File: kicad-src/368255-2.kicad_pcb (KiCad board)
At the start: 2 copper layers, 158 x 114 mm, 27 parts, among them J11 5569-08A2, J2 5569-18A2, J21 Conn_01x01_Pin, J22 Conn_01x01_Pin, J23 Conn_01x01_Pin, J24 Conn_01x01_Pin, J25 Conn_01x01_Pin, J26 Conn_01x01_Pin, J27 Conn_01x01_Pin, J28 Conn_01x01_Pin, J3 5569-06A2, J4 5569-16A2, J5 5569-20A2, P1 368255-2, U1 ULN2003A

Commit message: tracing refinement
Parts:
- added R10: 10k, Resistor_SMD:R_0201_0603Metric, F.Cu at (178.8, 92.0)
- added R8: 10k, Resistor_SMD:R_0201_0603Metric, F.Cu at (178.8, 93.0)
- added R9: 10k, Resistor_SMD:R_0201_0603Metric, F.Cu at (178.8, 90.6)
- J5: value 5569-20A2 -> 5569-20A2-new
- moved J25 1.45 mm to (169.3, 104.8)
- moved R1 0.80 mm to (172.9, 102.5), turned to 90 degrees
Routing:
- net /OUT_IGN1: track 144.2 -> 131.5 mm
- net GND: track 248.4 -> 254.8 mm
- net /BUTTON3: track 52.8 -> 58.7 mm
- net /OUT_INJ4: track 73.3 -> 67.7 mm
- net /IN_PPS2: track 175.6 -> 170.5 mm
- net /IN_BUTTON2: track 55.6 -> 59.0 mm
- net /OUT_DC2+: track 61.5 -> 58.7 mm
- net /CONTITIONER_ON: track 83.9 -> 86.3 mm
- net /5_WBO_Rtrim: track 146.4 -> 144.1 mm
- net /BUTTON1: track 50.6 -> 52.9 mm
- net +5VP: track 310.9 -> 309.4 mm
- net /CLUTCH_SENSOR: track 42.3 -> 43.7 mm
- net /OUT_IGN3: track 247.1 -> 245.8 mm
- net Net-(J25-Pin_1): track 8.99 -> 8.09 mm
- net /OUT_IGN2: track 151.2 -> 152.1 mm
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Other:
- board text added: "+5V_USB"
- board text added: "D+"
- board text added: "D-"
- board text added: "GND"

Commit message: tracing
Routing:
- net /OUT_LS3: track 73.7 -> 68.9 mm, vias 1 -> 0
- net GNDA: track 251.1 -> 246.8 mm
- net /5_WBO_Rtrim: track 144.1 -> 145.8 mm
- net /IN_BUTTON2: track 59.0 -> 57.5 mm
- net GND: track 254.8 -> 253.7 mm
- net /OUT_IGN5: track 50.0 -> 49.4 mm

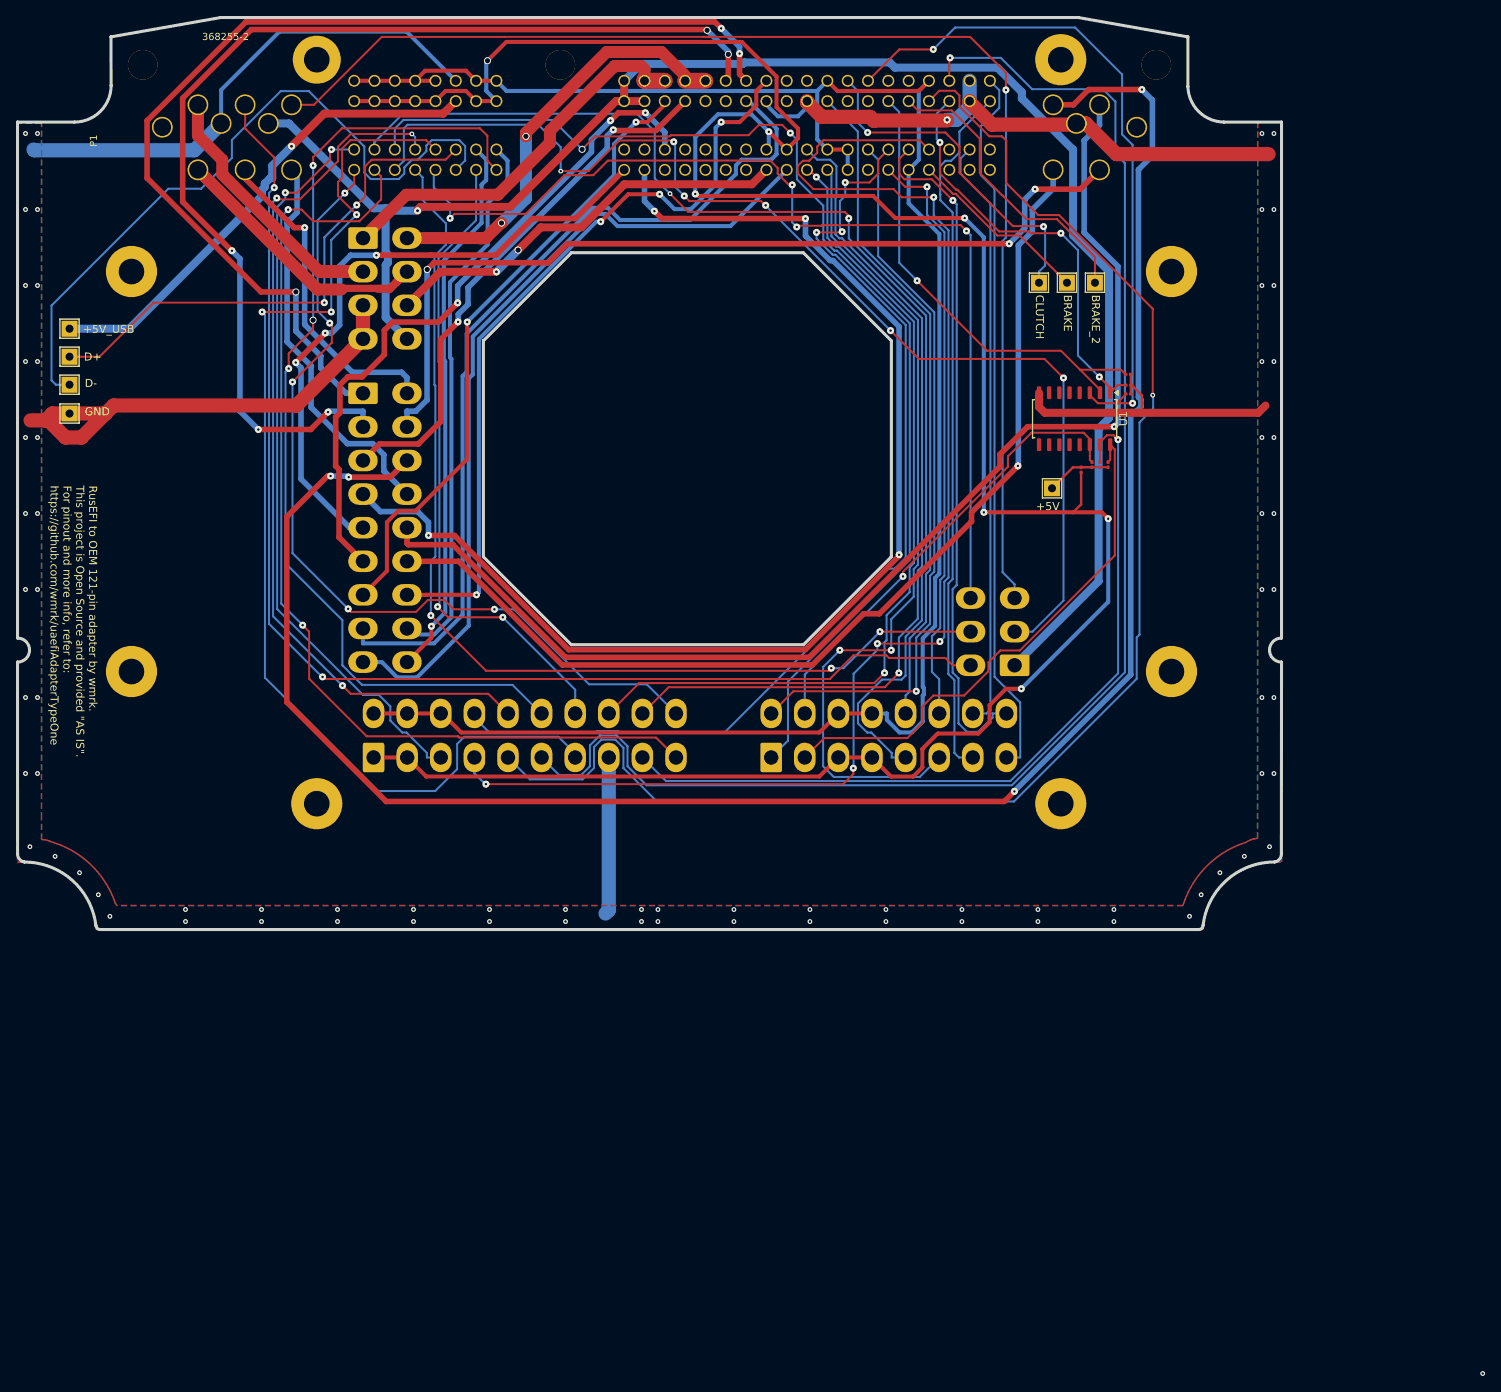
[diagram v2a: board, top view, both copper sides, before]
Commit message: net classes global fix
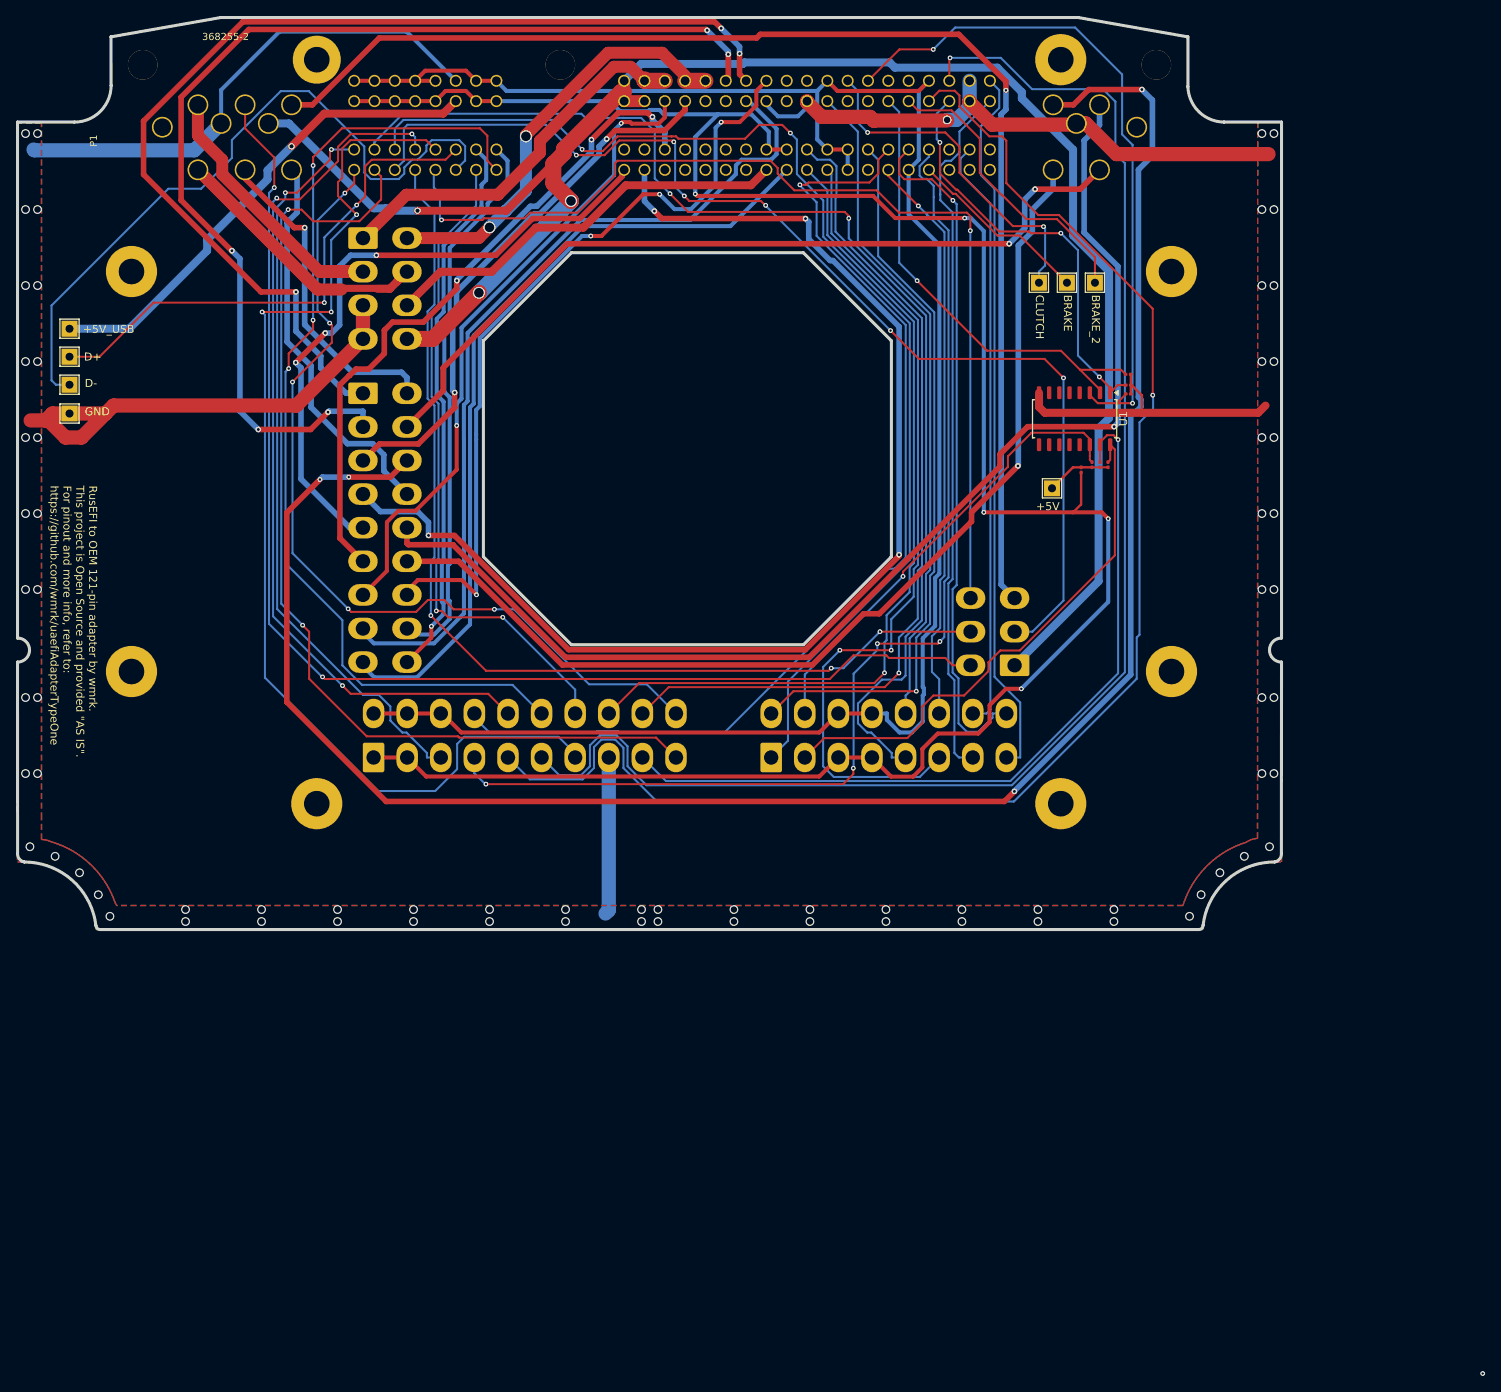
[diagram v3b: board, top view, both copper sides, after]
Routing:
- net /3_WBO_Heater: track 161.2 -> 202.4 mm
- net /IN_PPS2: track 170.5 -> 140.1 mm, vias 5 -> 4
- net +5VP: track 308.9 -> 281.9 mm, vias 7 -> 5
- net +12V: track 210.7 -> 227.0 mm, vias 1 -> 3
- net /OUT_IGN4: track 112.7 -> 103.6 mm, vias 3 -> 2
- net /5_WBO_Rtrim: track 145.8 -> 142.4 mm
- net /IN_TPS2: track 127.7 -> 130.3 mm, vias 3 -> 1
- net /OUT_LS1: track 79.4 -> 81.5 mm
- net /OUT_LS_HOT2: track 109.5 -> 107.4 mm
- net /OUT_LS4: track 96.9 -> 98.7 mm
- net /IN_KNOCK_RAW: track 73.5 -> 71.9 mm
- net /VR_MAX9924-: track 81.2 -> 82.3 mm
- net /OUT_LS_HOT1: track 102.2 -> 101.2 mm
- net /OUT_INJ1: track 85.5 -> 84.6 mm
- net /OUT_DC1-: track 49.3 -> 48.4 mm
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
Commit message: tracing
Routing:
- net /3_WBO_Heater: track 202.4 -> 164.3 mm
- net /IN_CLT: track 85.4 -> 79.0 mm
- net +12V: track 227.0 -> 231.7 mm
- net /OUT_LS4: track 98.7 -> 95.1 mm
- net /BRAKE_PEDAL_SENSOR: track 23.1 -> 25.7 mm
- net /CAN+: track 88.2 -> 90.5 mm
- net /IN_MAP: track 91.4 -> 89.4 mm
- net /EGT-: track 110.1 -> 108.5 mm
- net +5VP: track 281.9 -> 280.3 mm
- net /OUT_INJ3: track 153.0 -> 151.8 mm
- net /OUT_INJ2: track 80.8 -> 79.8 mm
- net /CAN-: track 89.8 -> 90.8 mm
- net /2_WBO_Vm: track 127.8 -> 126.8 mm
- net /IN_HALL3: track 140.7 -> 141.6 mm
- net /IN_PPS2: track 140.1 -> 139.4 mm
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
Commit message: trace
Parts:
- moved R1 0.80 mm to (172.9, 101.8), turned to -90 degrees
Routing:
- net +5VP: track 280.3 -> 257.5 mm, vias 5 -> 3
- net /IN_PPS1: track 104.0 -> 81.4 mm
- net /IN_TPS1: track 83.1 -> 94.5 mm
- net /IN_BUTTON1: track 67.5 -> 77.0 mm
- net /IN_PPS2: track 139.4 -> 133.2 mm, vias 4 -> 1
- net /5_WBO_Rtrim: track 142.4 -> 136.1 mm
- net /IN_BUTTON3: track 100.8 -> 96.1 mm
- net /VR_DISCRETE-: track 107.8 -> 104.4 mm
- net GNDA: track 246.8 -> 243.5 mm
- net /1_WBO_Ip: track 130.0 -> 126.9 mm, vias 3 -> 1
- net /VR_DISCRETE+: track 106.8 -> 103.9 mm
- net /IN_BUTTON2: track 57.5 -> 54.9 mm
- net /IN_CLT: track 79.0 -> 77.1 mm
- net /VR_MAX9924-: track 82.3 -> 80.6 mm
- net /IN_FLEX: track 150.9 -> 149.2 mm
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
